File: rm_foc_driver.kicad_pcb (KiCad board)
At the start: 4 copper layers, 70 x 70 mm, 88 parts, among them J1 SWD, J2 TMC4671, J3 UART, J4 TMC4671, J5 Conn_01x03, J6 Conn_01x02, J8 Conn_01x03, Q1 CSD18540Q5B, Q2 CSD18540Q5B, Q3 CSD18540Q5B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

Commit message: version 1.0.0-beta
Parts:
- removed C11, C9: 22pF, Capacitor_SMD:C_0603_1608Metric
- removed C34, C35, C36, C37: 100nF, Capacitor_SMD:C_0603_1608Metric
- removed C6: 4.7uF, Capacitor_SMD:C_0603_1608Metric
- removed D1, D2: LED, LED_SMD:LED_0603_1608Metric
- removed J4: TMC4671, Connector_PinHeader_2.54mm:PinHeader_1x04_P2.54mm_Vertical
- removed J5: Conn_01x03, Connector_PinSocket_2.54mm:PinSocket_1x03_P2.54mm_Vertical
- removed Y1: Crystal_GND24, Crystal:Crystal_SMD_3225-4Pin_3.2x2.5mm
- added R21: 10k, Resistor_SMD:R_0603_1608Metric, B.Cu at (171.7, 100.3)
- added R22: 10k, Resistor_SMD:R_0603_1608Metric, B.Cu at (171.6, 102.1)
- added REF**: ESD-Logo_6.6x6mm_SilkScreen, Symbol:ESD-Logo_6.6x6mm_SilkScreen, F.Cu at (167.6, 101.6)
- added REF**: OSHW-Logo_7.5x8mm_SilkScreen, Symbol:OSHW-Logo_7.5x8mm_SilkScreen, F.Cu at (175.3, 102.9)
- C4: value 100nF -> 1uF
- J1: value SWD -> TMC4671; footprint Connector_PinHeader_2.54mm:PinHeader_1x04_P2.54mm_Horizontal -> Connector_PinHeader_2.54mm:PinHeader_1x04_P2.54mm_Vertical
- J3: value UART -> Conn_01x03; footprint Connector_PinHeader_2.54mm:PinHeader_1x04_P2.54mm_Horizontal -> Connector_PinHeader_2.54mm:PinHeader_1x03_P2.54mm_Vertical
- U3: value STM32F401CCUx -> ADS1115IDGS; footprint Package_DFN_QFN:QFN-48-1EP_7x7mm_P0.5mm_EP5.6x5.6mm -> Package_SO:TSSOP-10_3x3mm_P0.5mm
- moved J1 22.4 mm to (158.1, 117.0)
- moved C4 19.8 mm to (168.3, 112.0)
- moved R5 16.3 mm to (157.2, 110.0)
- moved J3 15.7 mm to (168.3, 117.0)
- moved R1 11.6 mm to (157.2, 111.8), turned to 0 degrees
- moved U3 10.8 mm to (162.8, 110.7)
- moved R4 8.38 mm to (168.3, 110.2), turned to 180 degrees
- moved R3 8.13 mm to (168.3, 108.5), turned to 180 degrees
- moved U6 3.10 mm to (147.3, 111.0)
- moved C15 3.06 mm to (152.1, 111.0)
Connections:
- C4 pad 1: Net-(C4-Pad1) -> +5V
- J1 pad 1: +3.3V -> /RDY
- J1 pad 2: /SWDIO -> /SCL1
- J1 pad 3: /SWCLK -> /SDA1
- J3 pad 1: +5V -> /SCL2
- J3 pad 2: /TXD -> /SDA2
- J3 pad 3: /RXD -> GND
- R1 pad 1: Net-(C4-Pad1) -> +5V
- R1 pad 2: +3.3V -> /RDY
- R3 pad 1: Net-(R3-Pad1) -> +5V
- R3 pad 2: GND -> /SCL1
- R4 pad 1: +3.3V -> +5V
- R4 pad 2: Net-(D1-Pad2) -> /SDA1
- R5 pad 1: +3.3V -> GND
- R5 pad 2: Net-(D2-Pad2) -> Net-(R5-Pad2)
- U3 pad 1: +3.3V -> Net-(R5-Pad2)
- U3 pad 10: /SO1 -> /SCL1
- U3 pad 2: unconnected-(U3-Pad2) -> /RDY
- U3 pad 3: unconnected-(U3-Pad3) -> GND
- U3 pad 4: unconnected-(U3-Pad4) -> /SO1
- U3 pad 5: /OSC_IN -> /SO2
- U3 pad 6: /OSC_OUT -> unconnected-(U3-Pad6)
- U3 pad 7: Net-(C4-Pad1) -> unconnected-(U3-Pad7)
- U3 pad 8: GND -> +5V
- U3 pad 9: +3.3V -> /SDA1
- U7 pad 6: /MISO -> /SDA2
- U7 pad 7: /SCLK -> /SCL2
- U7 pad 8: /CS1 -> +5V
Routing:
- net +3.3V: track 106.9 -> 6.38 mm, vias 14 -> 6
- net /CS1: track 69.0 -> 0.00 mm, vias 1 -> 0
- net /SCLK: track 54.3 -> 0.00 mm
- net /MISO: track 53.5 -> 0.00 mm
- net /RXD: track 21.7 -> 0.00 mm
- net /SDA2: track 0.00 -> 21.5 mm
- net /SO2: track 40.4 -> 19.2 mm, vias 1 -> 0
- net /SCL2: track 0.00 -> 21.0 mm
- net /SDA1: track 0.00 -> 20.8 mm
- net /SCL1: track 0.00 -> 18.8 mm
- net /SWCLK: track 17.7 -> 0.00 mm, vias 1 -> 0
- net /TXD: track 17.5 -> 0.00 mm
- net /SWDIO: track 16.6 -> 0.00 mm, vias 1 -> 0
- net Net-(D1-Pad1): track 15.9 -> 0.00 mm
- net Net-(R3-Pad1): track 14.1 -> 0.00 mm
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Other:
- board size 70 x 70 mm -> 70 x 53.2 mm
- board text added: "Anlogic"
- board text added: "FPGA Competition"
- board text added: "PHY"
- board text added: "SCL1"
- board text added: "SDA1"
- board text added: "SDA2"
- board text removed: "+5V"
- board text removed: "A"
- board text removed: "B"
- board text removed: "DIO"
- board text removed: "RXD"
- board text removed: "SCK"
- board text removed: "TXD"
- board text removed: "VCC"
- board text removed: "Z"

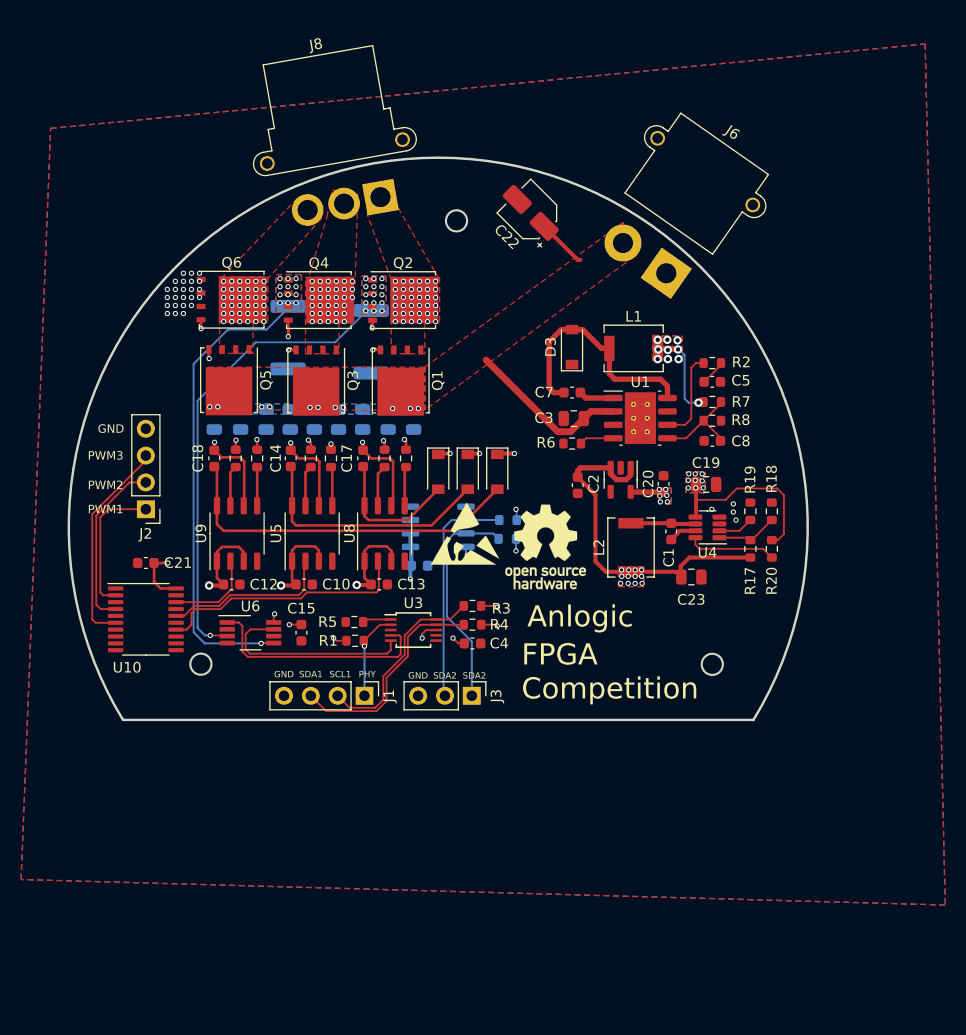
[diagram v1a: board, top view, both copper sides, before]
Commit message: version 1.0.0-beta.Round-angle PCB-layout
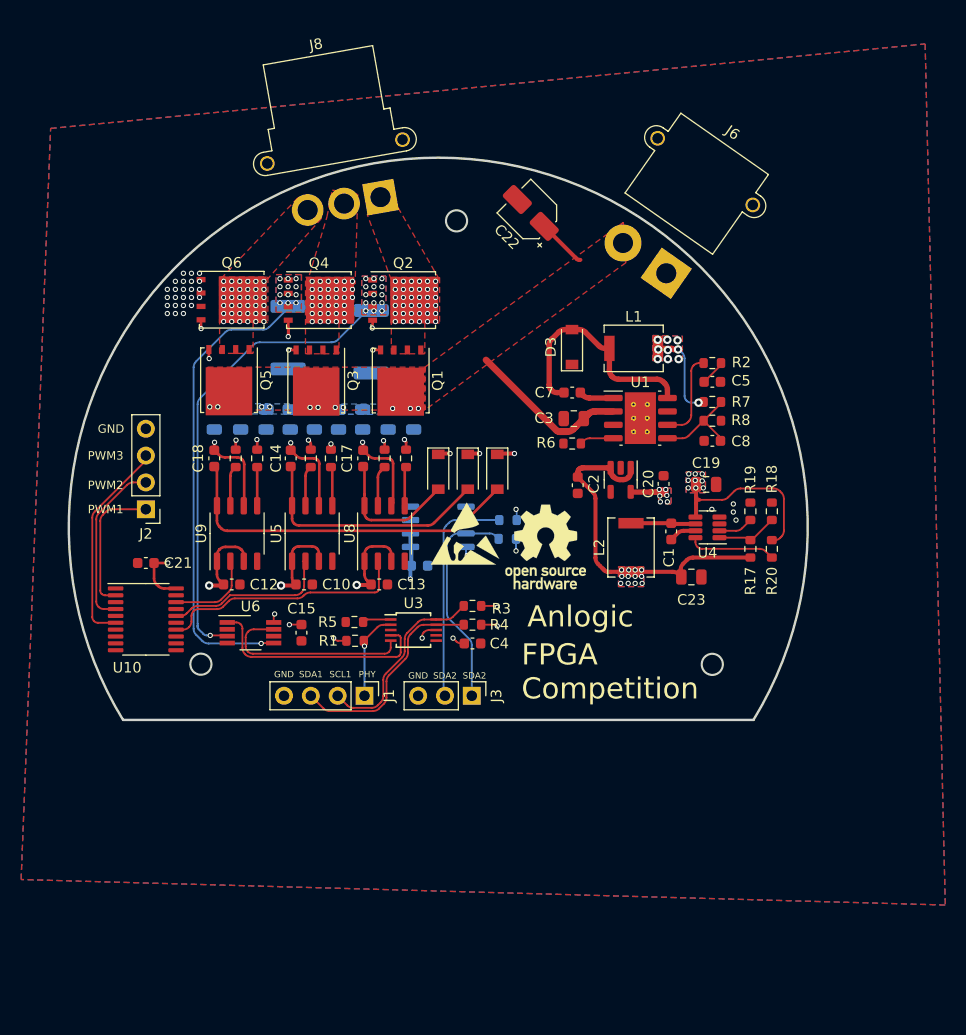
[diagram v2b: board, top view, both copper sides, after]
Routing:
- net +5V: track 139.8 -> 138.8 mm
- net Net-(C7-Pad2): track 22.5 -> 22.0 mm
